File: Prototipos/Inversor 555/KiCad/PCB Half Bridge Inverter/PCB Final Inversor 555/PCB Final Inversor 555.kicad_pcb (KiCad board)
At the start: 2 copper layers, 50 x 100 mm, 28 parts, among them Q1 IRFZ44, Q2 IRFZ44, Q3 BC548, U1 TLC555xD, U2 LM7809_TO220

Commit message: Corregir MHs PCB Inversor 555
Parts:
- M5_BotL, M5_TopL: renamed from REF**; value MountingHole_6.4mm_M6 -> MountingHole_5.3mm_M5; footprint MountingHole:MountingHole_6.4mm_M6 -> MountingHole:MountingHole_5.3mm_M5
- M5_BotR, M5_TopR: renamed from REF**; value MountingHole_4.3mm_M4 -> MountingHole_5.3mm_M5; footprint MountingHole:MountingHole_4.3mm_M4 -> MountingHole:MountingHole_5.3mm_M5
- moved M5_TopR 1.41 mm to (95.5, 52.6)
- moved M5_TopL 1.41 mm to (55.5, 52.6)
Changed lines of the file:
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@@
 		(embedded_fonts no)
 	)
-	(footprint "MountingHole:MountingHole_6.4mm_M6"
+	(footprint "MountingHole:MountingHole_5.3mm_M5"
 		(locked yes)
 		(layer "F.Cu")
-		(at 54.51 51.65)
-		(descr "Mounting Hole 6.4mm, no annular, M6")
-		(tags "mounting hole 6.4mm no annular m6")
-		(property "Reference" "REF**"
-			(at 0 -7.4 0)
-			(layer "F.SilkS")
-			(effects
-				(font
-					(size 1 1)
-					(thickness 0.15)
-				)
-			)
-		)
-		(property "Value" "MountingHole_6.4mm_M6"
-			(at 0 7.4 0)
+		(at 55.5 52.65)
+		(descr "Mounting Hole 5.3mm, M5, no annular, generated by kicad-footprint-generator mountinghole.py")
+		(tags "mountinghole M5")
+		(property "Reference" "M5_TopL"
+			(at 0 -3.907285 0)
+			(layer "F.SilkS")
+			(effects
+				(font
+					(size 1 1)
+					(thickness 0.15)
+				)
+			)
+		)
+		(property "Value" "MountingHole_5.3mm_M5"
+			(at 0 6.25 0)
 			(layer "F.Fab")
 			(effects
@@
 		(property "Datasheet" ""
 			(at 0 0 0)
-			(unlocked yes)
 			(layer "F.Fab")
 			(hide yes)
@@
 		(property "Description" ""
 			(at 0 0 0)
-			(unlocked yes)
 			(layer "F.Fab")
 			(hide yes)
@@
 		(fp_circle
 			(center 0 0)
-			(end 6.4 0)
+			(end 5.3 0)
 			(stroke
 				(width 0.15)
@@
 		(fp_circle
 			(center 0 0)
-			(end 6.65 0)
+			(end 5.55 0)
 			(stroke
 				(width 0.05)
@@
 		)
 		(pad "" np_thru_hole circle
-			(at 0 0)
-			(size 6.4 6.4)
-			(drill 6.4)
+			(at 0.01 0)
+			(size 5.3 5.3)
+			(drill 5.3)
 			(layers "*.Cu" "*.Mask")
 		)
@@
 		)
 	)
-	(footprint "MountingHole:MountingHole_6.4mm_M6"
+	(footprint "MountingHole:MountingHole_5.3mm_M5"
 		(locked yes)
 		(layer "F.Cu")
 		(at 54.51 143.65)
-		(descr "Mounting Hole 6.4mm, no annular, M6")
-		(tags "mounting hole 6.4mm no annular m6")
-		(property "Reference" "REF**"
-			(at 0 -7.4 0)
-			(layer "F.SilkS")
-			(effects
-				(font
-					(size 1 1)
-					(thickness 0.15)
-				)
-			)
-		)
-		(property "Value" "MountingHole_6.4mm_M6"
-			(at 0 7.4 0)
+		(descr "Mounting Hole 5.3mm, M5, no annular, generated by kicad-footprint-generator mountinghole.py")
+		(tags "mountinghole M5")
+		(property "Reference" "M5_BotL"
+			(at -0.01 -4.15 0)
+			(layer "F.SilkS")
+			(effects
+				(font
+					(size 1 1)
+					(thickness 0.15)
+				)
+			)
+		)
+		(property "Value" "MountingHole_5.3mm_M5"
+			(at 0 6.25 0)
 			(layer "F.Fab")
 			(effects
@@
 		(property "Datasheet" ""
 			(at 0 0 0)
-			(unlocked yes)
 			(layer "F.Fab")
 			(hide yes)
@@
 		(property "Description" ""
 			(at 0 0 0)
-			(unlocked yes)
 			(layer "F.Fab")
 			(hide yes)
@@
 		(fp_circle
 			(center 0 0)
-			(end 6.4 0)
+			(end 5.3 0)
 			(stroke
 				(width 0.15)
@@
 		(fp_circle
 			(center 0 0)
-			(end 6.65 0)
+			(end 5.55 0)
 			(stroke
 				(width 0.05)
@@
 		)
 		(fp_text user "${REFERENCE}"
-			(at 0 0 0)
+			(at 0 -4.15 0)
 			(layer "F.Fab")
 			(effects
@@
 		(pad "" np_thru_hole circle
 			(at 0 0)
-			(size 6.4 6.4)
-			(drill 6.4)
+			(size 5.3 5.3)
+			(drill 5.3)
 			(layers "*.Cu" "*.Mask")
 		)
@@
 		)
 	)
-	(footprint "MountingHole:MountingHole_4.3mm_M4"
+	(footprint "MountingHole:MountingHole_5.3mm_M5"
 		(locked yes)
 		(layer "F.Cu")
 		(at 96.51 143.65)
-		(descr "Mounting Hole 4.3mm, no annular, M4")
-		(tags "mounting hole 4.3mm no annular m4")
-		(property "Reference" "REF**"
-			(at 0 -5.3 0)
-			(layer "F.SilkS")
-			(effects
-				(font
-					(size 1 1)
-					(thickness 0.15)
-				)
-			)
-		)
-		(property "Value" "MountingHole_4.3mm_M4"
-			(at 0 5.3 0)
+		(descr "Mounting Hole 5.3mm, M5, no annular, generated by kicad-footprint-generator mountinghole.py")
+		(tags "mountinghole M5")
+		(property "Reference" "M5_BotR"
+			(at -0.01 -4.15 0)
+			(layer "F.SilkS")
+			(effects
+				(font
+					(size 1 1)
+					(thickness 0.15)
+				)
+			)
+		)
+		(property "Value" "MountingHole_5.3mm_M5"
+			(at 0 6.25 0)
 			(layer "F.Fab")
 			(effects
@@
 		(property "Datasheet" ""
 			(at 0 0 0)
-			(unlocked yes)
 			(layer "F.Fab")
 			(hide yes)
@@
 		(property "Description" ""
 			(at 0 0 0)
-			(unlocked yes)
 			(layer "F.Fab")
 			(hide yes)
@@
 		(fp_circle
 			(center 0 0)
-			(end 4.3 0)
+			(end 5.3 0)
 			(stroke
 				(width 0.15)
@@
 		(fp_circle
 			(center 0 0)
-			(end 4.55 0)
+			(end 5.55 0)
 			(stroke
 				(width 0.05)
@@
 		(pad "" np_thru_hole circle
 			(at 0 0)
-			(size 4.3 4.3)
-			(drill 4.3)
+			(size 5.3 5.3)
+			(drill 5.3)
 			(layers "*.Cu" "*.Mask")
 		)
@@
 		)
 	)
-	(footprint "MountingHole:MountingHole_4.3mm_M4"
+	(footprint "MountingHole:MountingHole_5.3mm_M5"
 		(locked yes)
 		(layer "F.Cu")
-		(at 96.51 51.65)
-		(descr "Mounting Hole 4.3mm, no annular, M4")
-		(tags "mounting hole 4.3mm no annular m4")
-		(property "Reference" "REF**"
-			(at 0 -5.3 0)
-			(layer "F.SilkS")
-			(effects
-				(font
-					(size 1 1)
-					(thickness 0.15)
-				)
-			)
-		)
-		(property "Value" "MountingHole_4.3mm_M4"
-			(at 0 5.3 0)
+		(at 95.51 52.65)
+		(descr "Mounting Hole 5.3mm, M5, no annular, generated by kicad-footprint-generator mountinghole.py")
+		(tags "mountinghole M5")
+		(property "Reference" "M5_TopR"
+			(at 0.042152 -3.916785 0)
+			(layer "F.SilkS")
+			(effects
+				(font
+					(size 1 1)
+					(thickness 0.15)
+				)
+			)
+		)
+		(property "Value" "MountingHole_5.3mm_M5"
+			(at 0 6.25 0)
 			(layer "F.Fab")
 			(effects
@@
 		(property "Datasheet" ""
 			(at 0 0 0)
-			(unlocked yes)
 			(layer "F.Fab")
 			(hide yes)
@@
 		(property "Description" ""
 			(at 0 0 0)
-			(unlocked yes)
 			(layer "F.Fab")
 			(hide yes)
@@
 		(fp_circle
 			(center 0 0)
-			(end 4.3 0)
+			(end 5.3 0)
 			(stroke
 				(width 0.15)
@@
 		(fp_circle
 			(center 0 0)
-			(end 4.55 0)
+			(end 5.55 0)
 			(stroke
 				(width 0.05)
@@
 		(pad "" np_thru_hole circle
 			(at 0 0)
-			(size 4.3 4.3)
-			(drill 4.3)
+			(size 5.3 5.3)
+			(drill 5.3)
 			(layers "*.Cu" "*.Mask")
 		)

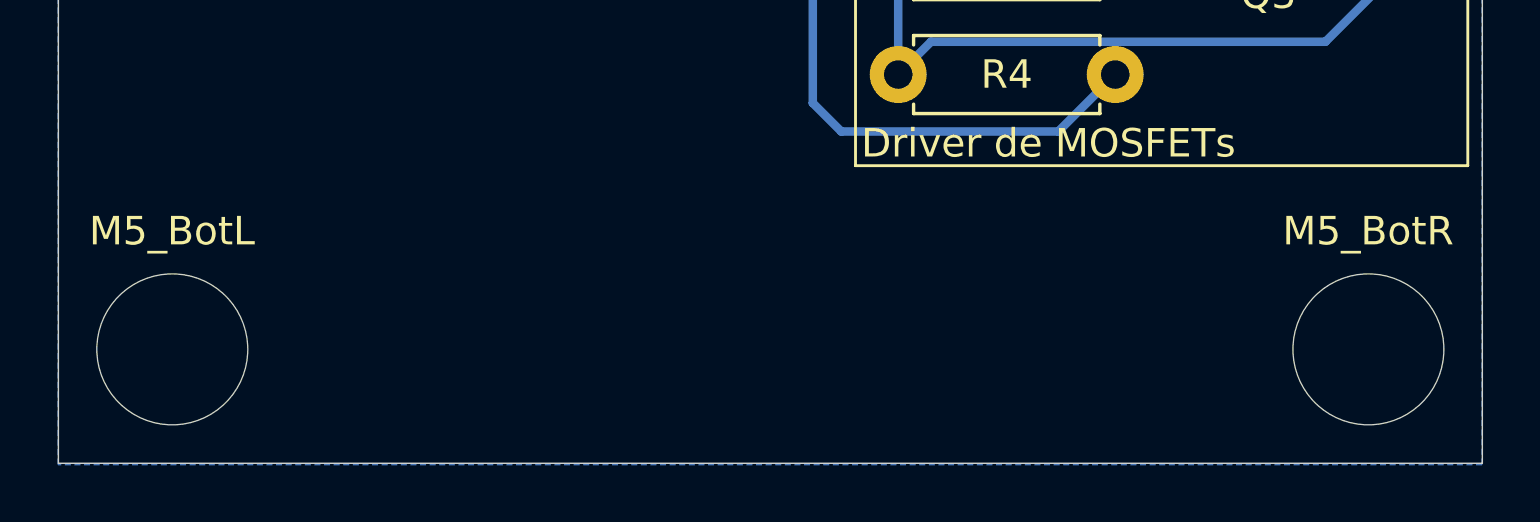
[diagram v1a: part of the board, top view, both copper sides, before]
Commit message: Corregir bordes inferiores
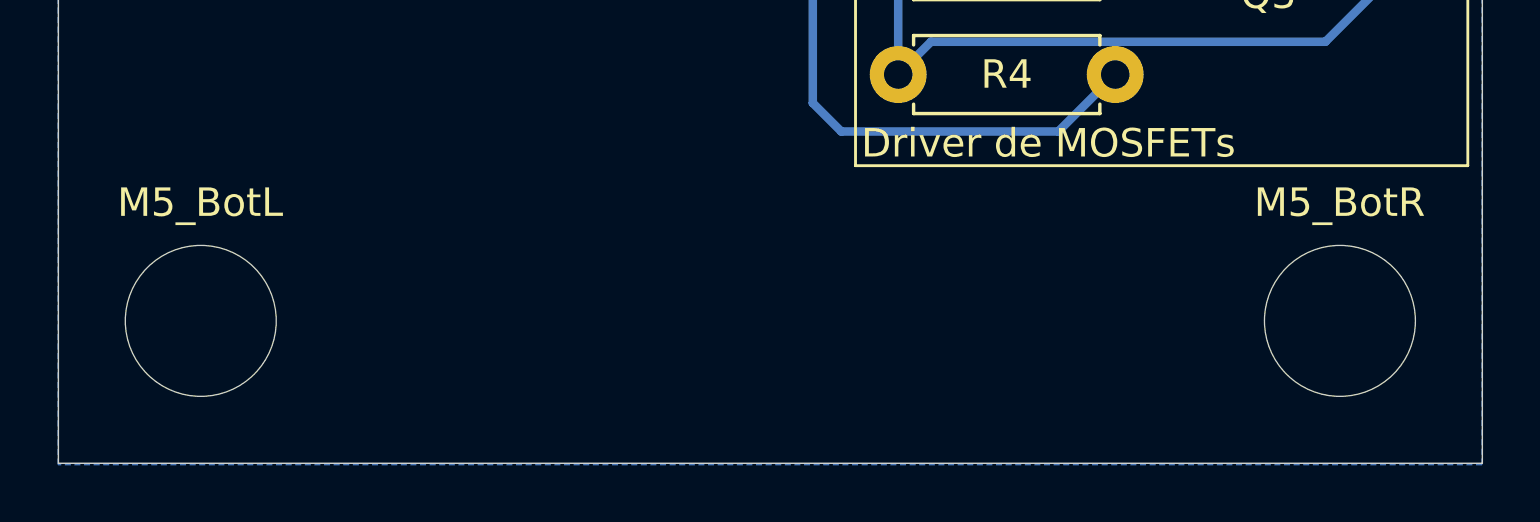
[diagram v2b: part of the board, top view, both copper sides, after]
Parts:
- moved M5_BotL 1.41 mm to (55.5, 142.7)
- moved M5_BotR 1.41 mm to (95.5, 142.7)
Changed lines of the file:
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@@
 		(locked yes)
 		(layer "F.Cu")
-		(at 54.51 143.65)
+		(at 55.51 142.65)
 		(descr "Mounting Hole 5.3mm, M5, no annular, generated by kicad-footprint-generator mountinghole.py")
 		(tags "mountinghole M5")
 		(property "Reference" "M5_BotL"
-			(at -0.01 -4.15 0)
+			(at -0.02 -4.15 0)
 			(layer "F.SilkS")
 			(effects
@@
 		)
 		(fp_text user "${REFERENCE}"
-			(at 0 -4.15 0)
+			(at -0.01 -4.15 0)
 			(layer "F.Fab")
 			(effects
@@
 		(locked yes)
 		(layer "F.Cu")
-		(at 96.51 143.65)
+		(at 95.51 142.65)
 		(descr "Mounting Hole 5.3mm, M5, no annular, generated by kicad-footprint-generator mountinghole.py")
 		(tags "mountinghole M5")

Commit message: Corregir errores y warnings
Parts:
- moved R6 0.50 mm to (87.6, 125.5)
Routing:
- net PGND: track 171.4 -> 163.0 mm

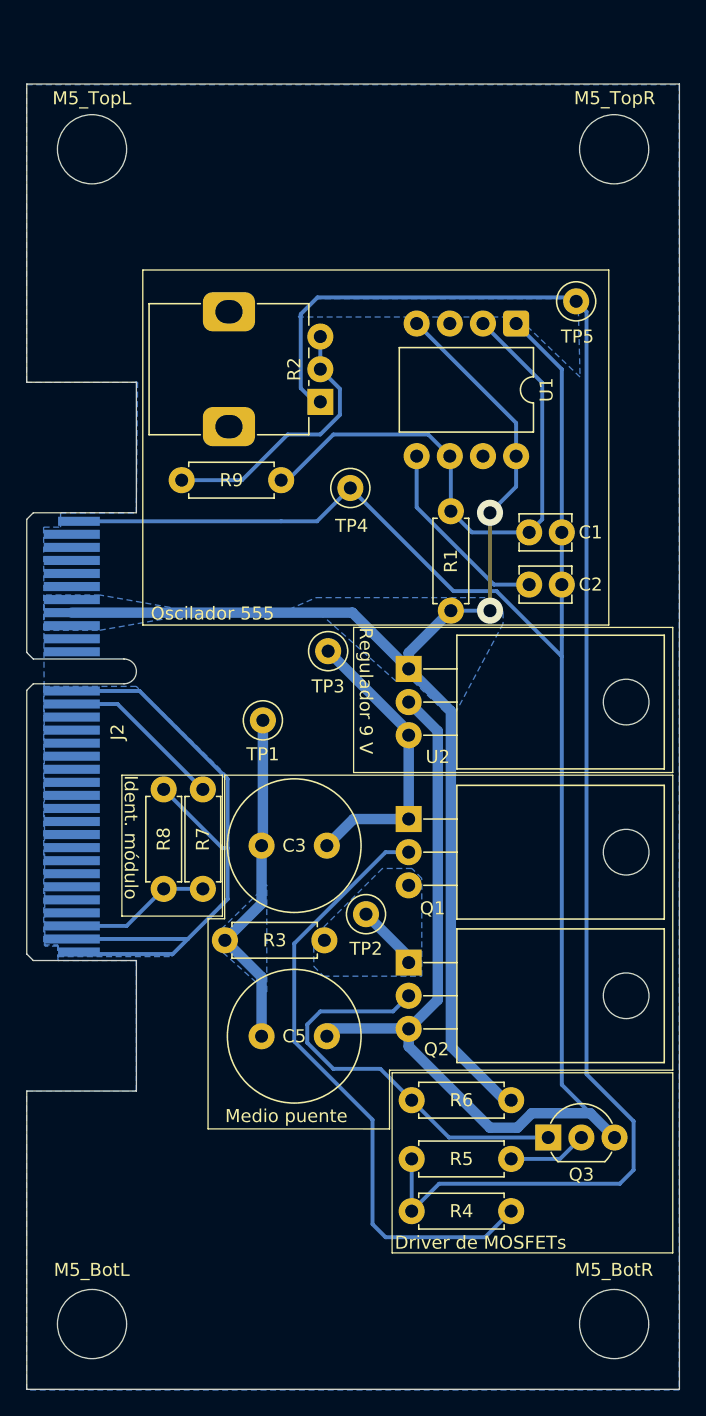
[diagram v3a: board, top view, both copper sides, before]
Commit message: Modificaciones en esquemático y PCB inversor medio puente.
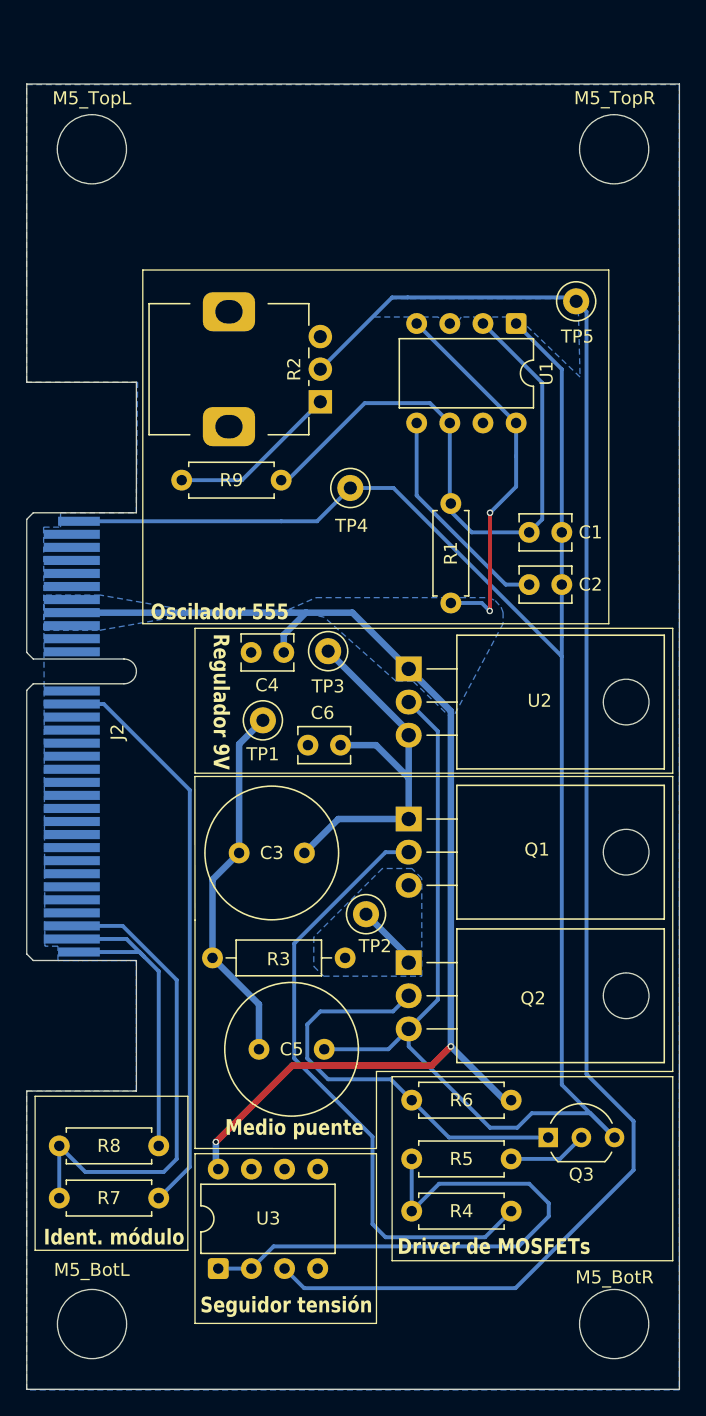
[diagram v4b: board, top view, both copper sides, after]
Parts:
- added C4: 0.33u, Capacitor_THT:C_Disc_D3.8mm_W2.6mm_P2.50mm, F.Cu at (70.2, 91.2)
- added C6: 0.1u, Capacitor_THT:C_Disc_D3.8mm_W2.6mm_P2.50mm, F.Cu at (74.5, 98.3)
- added U3: LM358, Package_DIP:DIP-8_W7.62mm, F.Cu at (65.2, 138.4)
- C3, C5: value 1200u -> 1500u
- R3: footprint Resistor_THT:R_Axial_DIN0207_L6.3mm_D2.5mm_P7.62mm_Horizontal -> Resistor_THT:R_Axial_DIN0207_L6.3mm_D2.5mm_P10.16mm_Horizontal
- R4: value 100 -> 1.2k
- R5: value 5,6k -> 330k
- R6: value 120 -> 1.2k
- U1: footprint Package_DIP:DIP-8_W10.16mm -> Package_DIP:DIP-8_W7.62mm
- moved R7 31.5 mm to (60.6, 133.0), turned to 180 degrees
- moved R8 21.3 mm to (53.0, 129.0), turned to 0 degrees
- moved R1 8.21 mm to (83.0, 79.8), turned to -90 degrees
- moved R3 2.09 mm to (74.9, 114.6)
- moved C3 1.81 mm to (71.8, 106.6)
- moved C5 1.02 mm to (68.3, 121.6)
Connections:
- net Net-(Q1-D) renamed 9Vdc
- R1 pad 1: 12Vdc -> Net-(U1-THR)
- R1 pad 2: Net-(U1-THR) -> 12Vdc
- R2 pad 1: 555 -> Net-(R2-Pad2)
- R2 pad 2: Net-(R2-Pad2) -> 555
- R2 pad 3: Net-(R2-Pad2) -> (no net)
- R4 pad 1: 555 -> VF_Out
- R5 pad 1: 555 -> VF_Out
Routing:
- net VF_Out: track 0.00 -> 44.0 mm
- net 3,3Vdc: track 12.7 -> 44.0 mm
- net Module_ident: track 11.2 -> 37.7 mm
- net AGND: track 52.8 -> 26.4 mm
- net 12Vdc: track 99.0 -> 120.8 mm, vias 2 -> 4
- net 9Vdc: track 22.5 -> 30.7 mm
- net Net-(R2-Pad2): track 20.8 -> 13.6 mm
- net Net-(U1-THR): track 44.3 -> 47.4 mm
- net Net-(C3-Pad2): track 26.0 -> 28.3 mm
- net Net-(U1-CV): track 15.0 -> 17.0 mm
- net 555: track 120.3 -> 121.7 mm
- net PGND: track 163.0 -> 163.9 mm
- net Net-(Q2-G): track 31.5 -> 32.3 mm
- removed copper zone on B.Cu, net AGND
- removed copper zone on B.Cu, net Net-(C3-Pad2)
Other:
- board text added: "Regulador 9V"
- board text added: "Seguidor tensión"
- board text removed: "Regulador 9 V"

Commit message: Agregado de stitching
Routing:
- net AGND: track 26.4 -> 46.3 mm, vias 0 -> 10
- net PGND: vias 0 -> 108
- added copper zone on B.Cu, net AGND
- added copper zone on F.Cu, net AGND
- added copper zone on F.Cu, net PGND
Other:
- board text added: "Módulo inversor de onda cuadrada"
